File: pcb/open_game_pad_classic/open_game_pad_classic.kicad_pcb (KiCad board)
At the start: 2 copper layers, 140 x 70 mm, 41 parts, among them J1 COM-09032, J2 COM-09032, U1 MM74C923, U2 74HC4051, U3 SN74AHC1G04DBVR

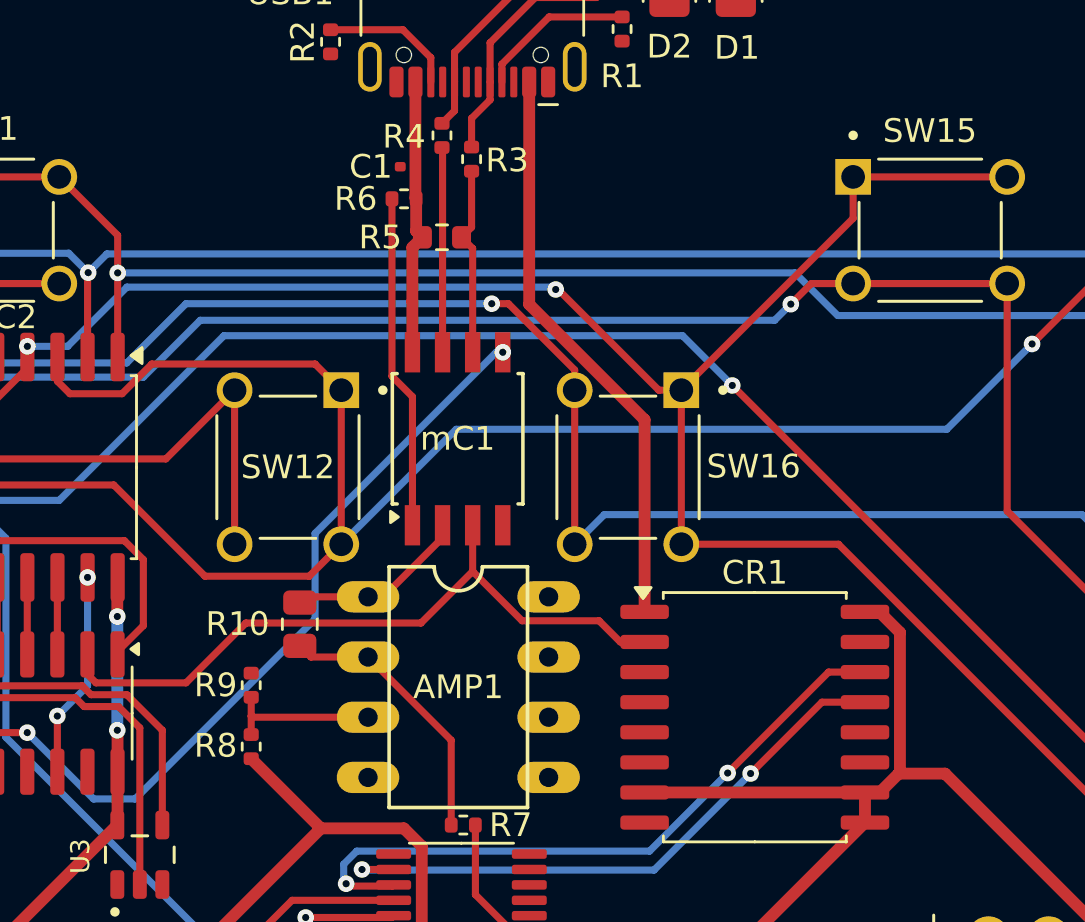
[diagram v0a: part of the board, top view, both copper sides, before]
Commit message: More decoupling for microcontroller and timer.
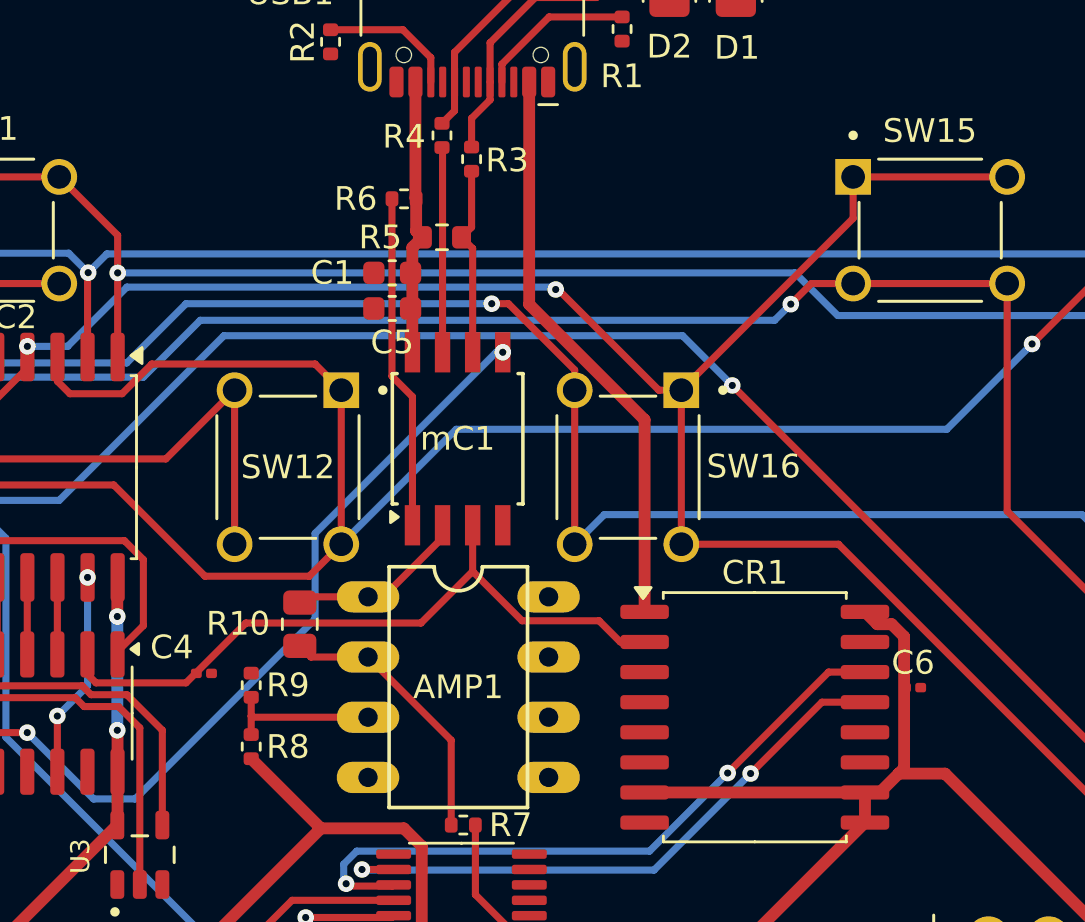
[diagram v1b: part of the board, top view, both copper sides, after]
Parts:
- added C4: 10 pF, Capacitor_SMD:C_0201_0603Metric, F.Cu at (134.4, 88.7)
- added C5: 10 µF, Capacitor_SMD:C_0603_1608Metric, F.Cu at (142.3, 73.3)
- added C6: 100nF, Capacitor_SMD:C_0201_0603Metric, F.Cu at (164.3, 89.3)
- C1: footprint Capacitor_SMD:C_0201_0603Metric -> Capacitor_SMD:C_0603_1608Metric
- moved C1 4.53 mm to (142.3, 71.8)

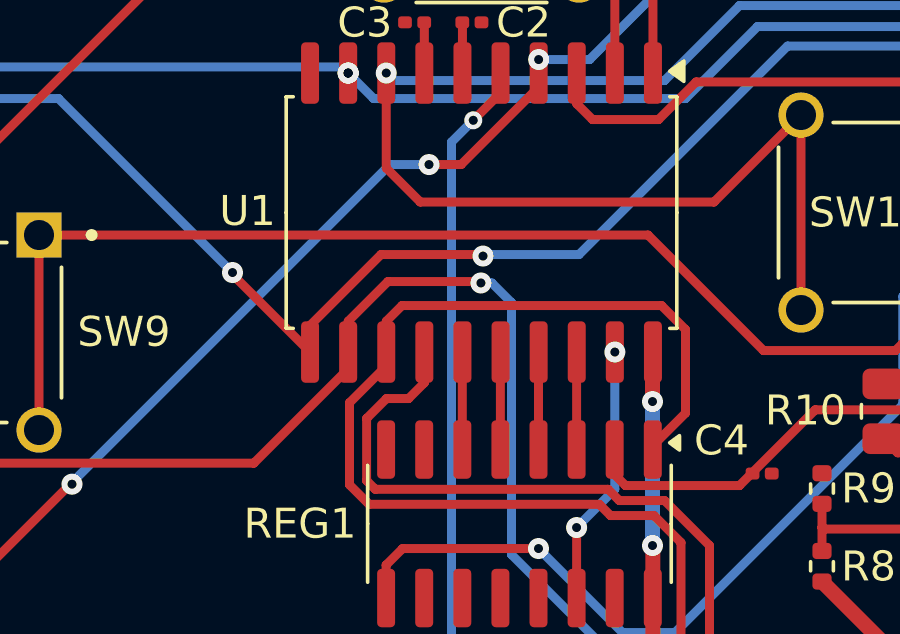
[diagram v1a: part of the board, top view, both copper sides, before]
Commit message: Fixed the schematic on PISO read. Updated the PCB.
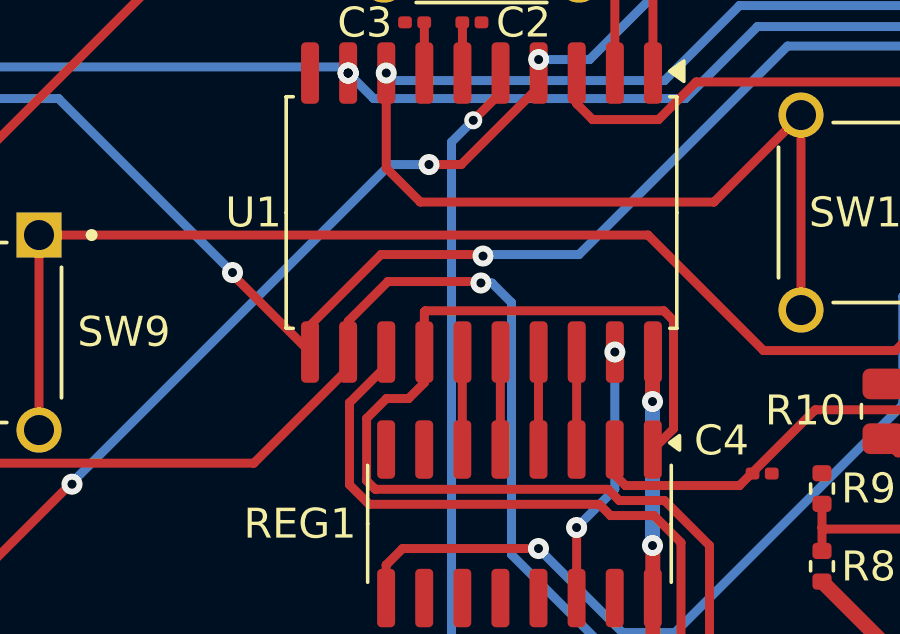
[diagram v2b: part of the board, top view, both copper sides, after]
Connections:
- U1 pad 13: Net-(REG1-~{PL}) -> Net-(U1-DA)
- U1 pad 14: Net-(U1-XOE) -> Net-(REG1-~{PL})
- U3 pad 2: Net-(REG1-~{PL}) -> Net-(U1-DA)
- U3 pad 4: Net-(U1-XOE) -> Net-(REG1-~{PL})
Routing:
- net Net-(U1-DA): track 0.00 -> 23.4 mm
- net Net-(U1-XOE): track 21.8 -> 0.00 mm
- net Net-(REG1-~{PL}): track 39.3 -> 36.2 mm

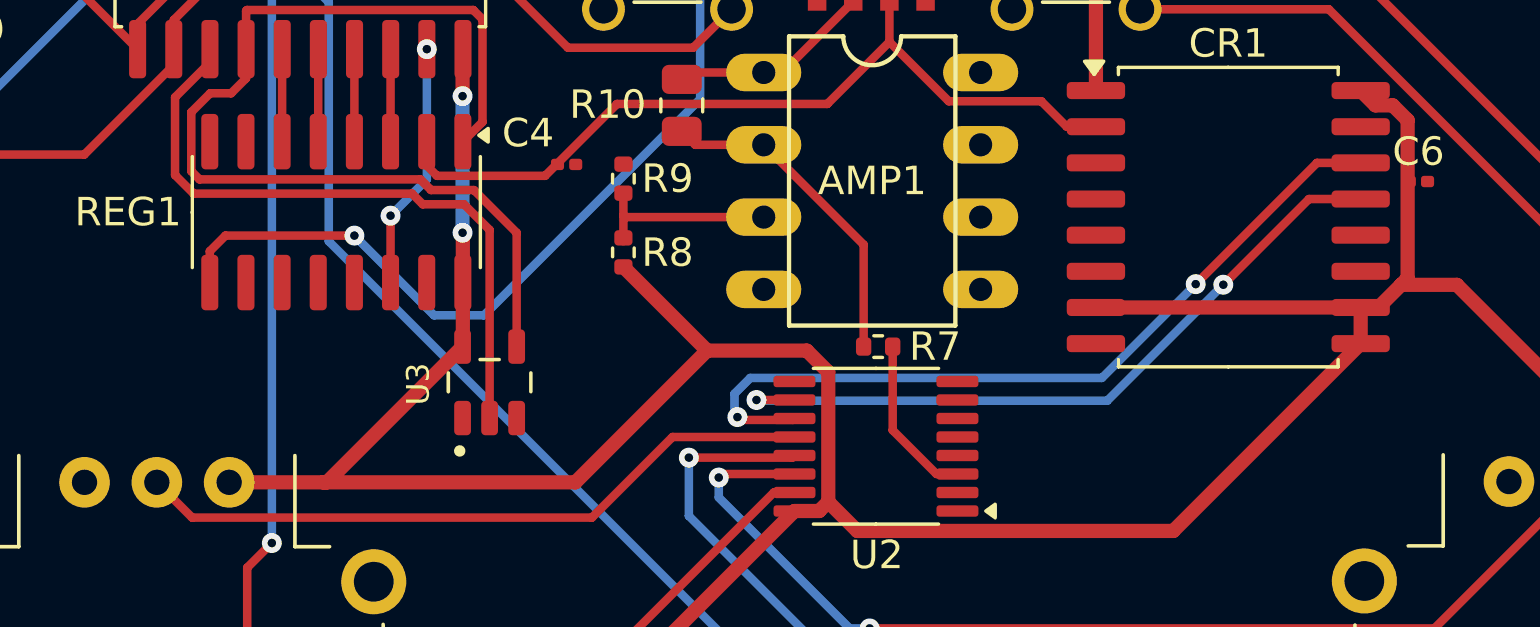
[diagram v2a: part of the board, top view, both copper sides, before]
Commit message: Fixed the reset problem by adding an 8-tick delay.
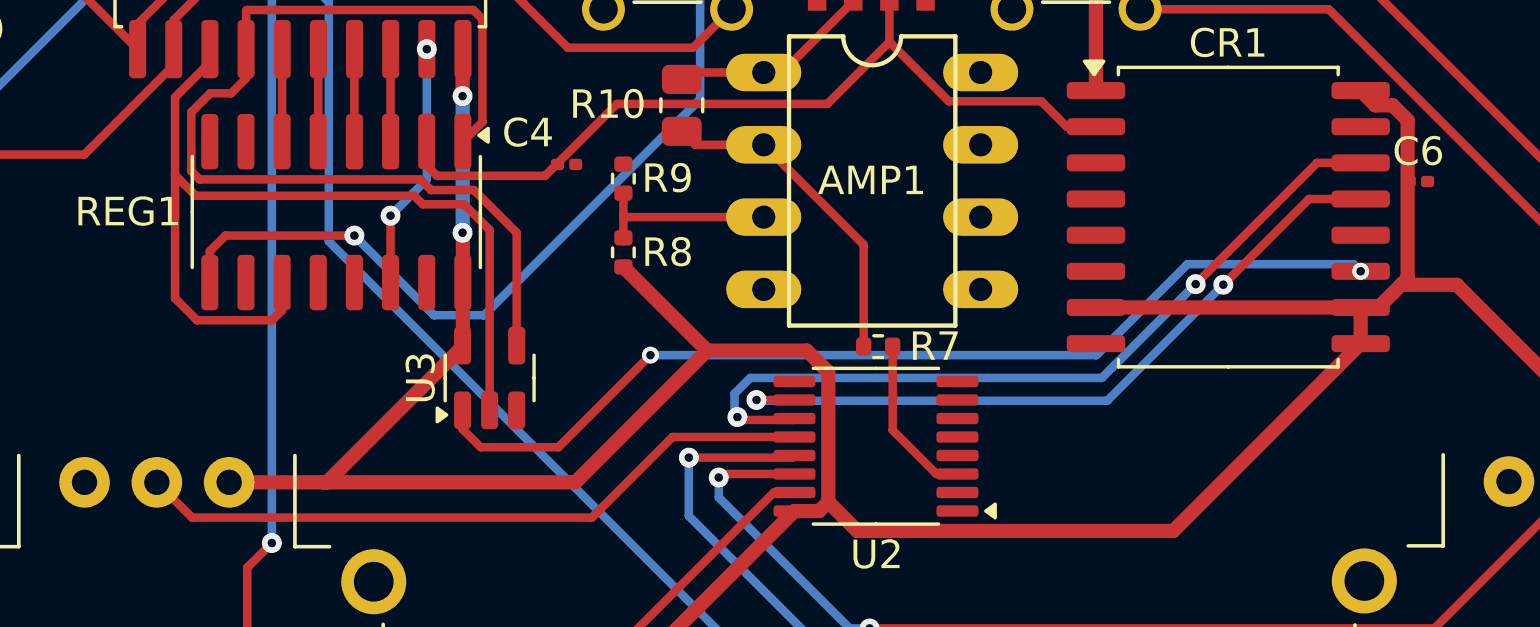
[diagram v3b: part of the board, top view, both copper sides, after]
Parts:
- U3: value SN74AHC1G04DBVR -> 74AHC1G00; footprint SN74AHC1G04DBVR:SOT95P280X145-5N -> Package_TO_SOT_SMD:SOT-23-5
- moved U3 0.16 mm to (131.7, 96.2)
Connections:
- CR1 pad 11: unconnected-(CR1-Q3-Pad11) -> /8TICK
- REG1 pad 11: GND -> Net-(REG1-D0)
- U1 pad 13: Net-(U1-DA) -> Net-(REG1-D0)
- U3 pad 1: unconnected-(U3-Pad1) -> /8TICK
- U3 pad 2: Net-(U1-DA) -> Net-(REG1-D0)
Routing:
- net /8TICK: track 0.00 -> 35.2 mm, vias 0 -> 2
- net Net-(REG1-D0): track 0.00 -> 32.9 mm
- net Net-(U1-DA): track 23.4 -> 0.00 mm

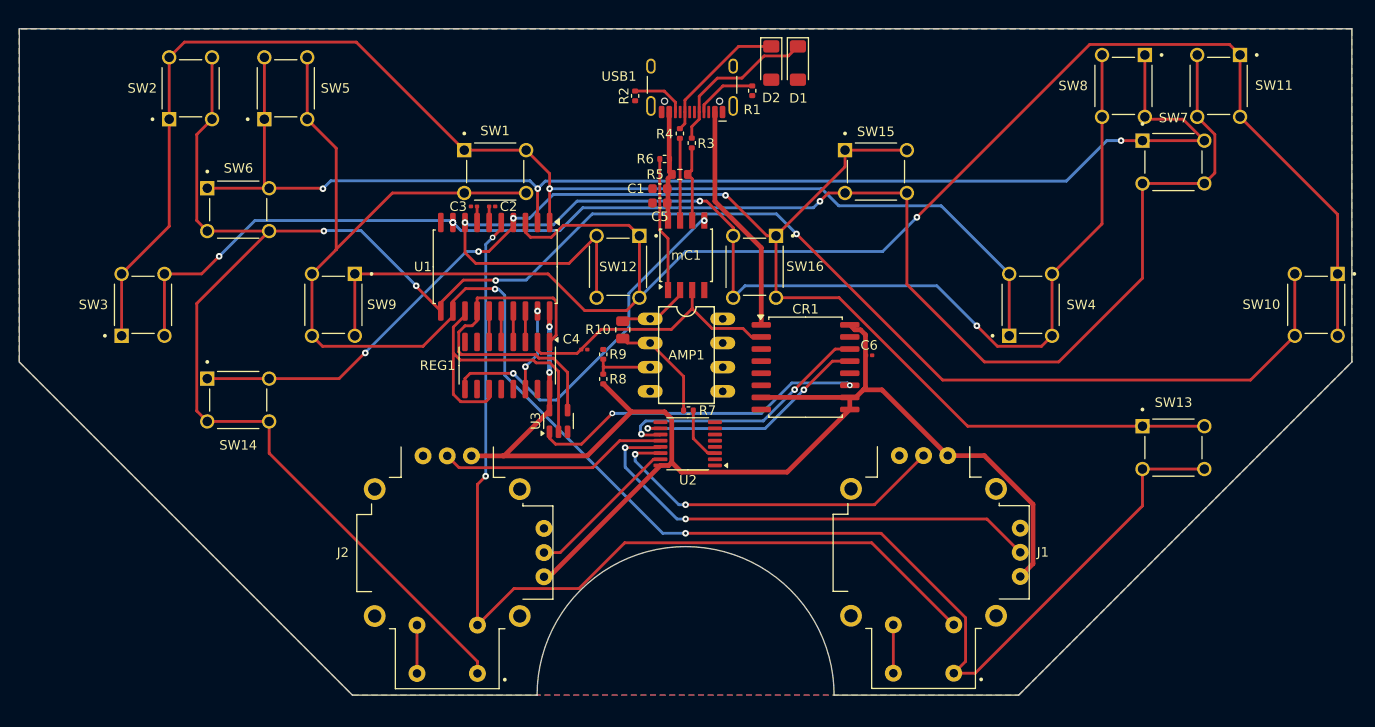
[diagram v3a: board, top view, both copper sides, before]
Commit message: Updated the PCB based on the new schematic design.
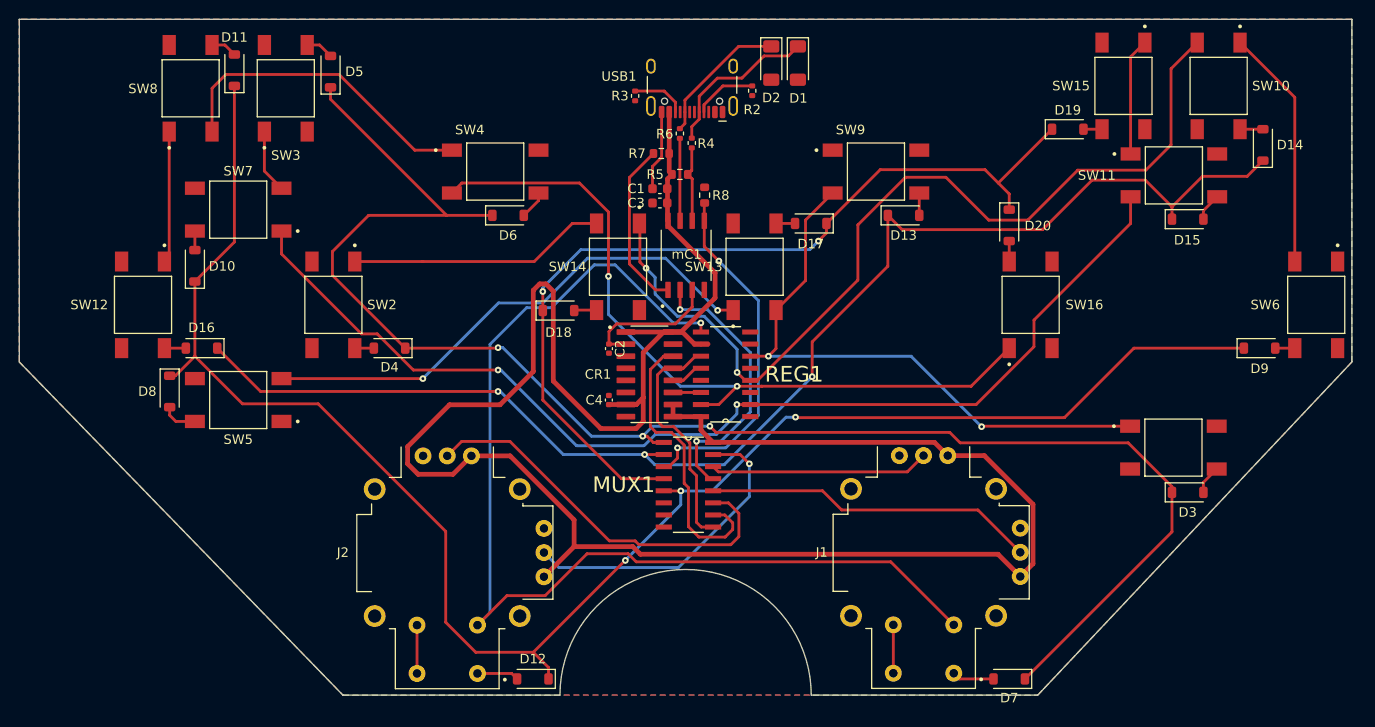
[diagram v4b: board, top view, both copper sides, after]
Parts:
- removed AMP1: LM358, LM358:DIL8
- removed the C3 at (122.8, 73.7)
- removed C6: 100nF, Capacitor_SMD:C_0201_0603Metric
- removed R10: R 10K, Resistor_SMD:R_0805_2012Metric
- removed the R7 at (145.3, 95.1)
- removed R9: R 4.7K, Resistor_SMD:R_0402_1005Metric
- removed U1: MM74C923, Package_SO:SOIC-20W_7.5x12.8mm_P1.27mm
- removed U2: 74HC4051, Package_SO:TSSOP-16_4.4x5mm_P0.65mm
- removed U3: 74AHC1G00, Package_TO_SOT_SMD:SOT-23-5
- added D10: 1N4148W, Diode_SMD:D_SOD-123, F.Cu at (93.5, 79.9)
- added D11: 1N4148W, Diode_SMD:D_SOD-123, F.Cu at (97.6, 59.4)
- added D12: 1N4148W, Diode_SMD:D_SOD-123, F.Cu at (128.9, 123.3)
- added D13: 1N4148W, Diode_SMD:D_SOD-123, F.Cu at (167.9, 74.6)
- added D14: 1N4148W, Diode_SMD:D_SOD-123, F.Cu at (205.7, 67.2)
- added D15: 1N4148W, Diode_SMD:D_SOD-123, F.Cu at (197.8, 75.0)
- added D16: 1N4148W, Diode_SMD:D_SOD-123, F.Cu at (94.2, 88.5)
- added D17: 1N4148W, Diode_SMD:D_SOD-123, F.Cu at (158.2, 75.5)
- added D18: 1N4148W, Diode_SMD:D_SOD-123, F.Cu at (131.7, 84.6)
- added D19: 1N4148W, Diode_SMD:D_SOD-123, F.Cu at (185.2, 65.5)
- added D20: 1N4148W, Diode_SMD:D_SOD-123, F.Cu at (179.0, 75.7)
- added D3: 1N4148W, Diode_SMD:D_SOD-123, F.Cu at (197.8, 103.7)
- added D4: 1N4148W, Diode_SMD:D_SOD-123, F.Cu at (113.9, 88.5)
- added D5: 1N4148W, Diode_SMD:D_SOD-123, F.Cu at (107.7, 59.5)
- added D6: 1N4148W, Diode_SMD:D_SOD-123, F.Cu at (126.3, 74.6)
- added D7: 1N4148W, Diode_SMD:D_SOD-123, F.Cu at (179.0, 123.3)
- added D8: 1N4148W, Diode_SMD:D_SOD-123, F.Cu at (90.8, 93.1)
- added D9: 1N4148W, Diode_SMD:D_SOD-123, F.Cu at (205.3, 88.5)
- added MUX1: 74HC4052D_653, 74HC4052D_653:SOIC127P600X175-16N, F.Cu at (145.3, 102.9)
- C2: value 0.01 mkF -> 10 pF; footprint Capacitor_SMD:C_0201_0603Metric -> Capacitor_SMD:C_0402_1005Metric
- C4: value 10 pF -> 100nF; footprint Capacitor_SMD:C_0201_0603Metric -> Capacitor_SMD:C_0402_1005Metric
- CR1: footprint Package_SO:SOIC-16W_7.5x10.3mm_P1.27mm -> SN74HC163DR:SOIC127P600X175-16N
- R7: renamed from R6; footprint Resistor_SMD:R_0402_1005Metric -> Resistor_SMD:R_0603_1608Metric
- R8: value R 4.7K -> R 1.5K; footprint Resistor_SMD:R_0402_1005Metric -> Resistor_SMD:R_0603_1608Metric
- REG1: value 74HC165 -> 74HC595; footprint Package_SO:SOIC-16_3.9x9.9mm_P1.27mm -> 74HC595DR:SOIC127P600X175-16N
- SW1: renamed from SW13; footprint TS02-66-95-BK-260-LCR-D:SW_TS02-66-95-BK-260-LCR-D -> TS04-66-95-BK-100-SMT:SW_TS04-66-95-BK-100-SMT
- SW10: renamed from SW11; footprint TS02-66-95-BK-260-LCR-D:SW_TS02-66-95-BK-260-LCR-D -> TS04-66-95-BK-100-SMT:SW_TS04-66-95-BK-100-SMT
- SW11: renamed from SW7; footprint TS02-66-95-BK-260-LCR-D:SW_TS02-66-95-BK-260-LCR-D -> TS04-66-95-BK-100-SMT:SW_TS04-66-95-BK-100-SMT
- SW12: renamed from SW3; footprint TS02-66-95-BK-260-LCR-D:SW_TS02-66-95-BK-260-LCR-D -> TS04-66-95-BK-100-SMT:SW_TS04-66-95-BK-100-SMT
- SW13: renamed from SW16; footprint TS02-66-95-BK-260-LCR-D:SW_TS02-66-95-BK-260-LCR-D -> TS04-66-95-BK-100-SMT:SW_TS04-66-95-BK-100-SMT
- SW14: renamed from SW12; footprint TS02-66-95-BK-260-LCR-D:SW_TS02-66-95-BK-260-LCR-D -> TS04-66-95-BK-100-SMT:SW_TS04-66-95-BK-100-SMT
- SW15: renamed from SW8; footprint TS02-66-95-BK-260-LCR-D:SW_TS02-66-95-BK-260-LCR-D -> TS04-66-95-BK-100-SMT:SW_TS04-66-95-BK-100-SMT
- SW16: renamed from SW4; footprint TS02-66-95-BK-260-LCR-D:SW_TS02-66-95-BK-260-LCR-D -> TS04-66-95-BK-100-SMT:SW_TS04-66-95-BK-100-SMT
- SW2: renamed from SW9; footprint TS02-66-95-BK-260-LCR-D:SW_TS02-66-95-BK-260-LCR-D -> TS04-66-95-BK-100-SMT:SW_TS04-66-95-BK-100-SMT
- SW3: renamed from SW5; footprint TS02-66-95-BK-260-LCR-D:SW_TS02-66-95-BK-260-LCR-D -> TS04-66-95-BK-100-SMT:SW_TS04-66-95-BK-100-SMT
- SW4: renamed from SW1; footprint TS02-66-95-BK-260-LCR-D:SW_TS02-66-95-BK-260-LCR-D -> TS04-66-95-BK-100-SMT:SW_TS04-66-95-BK-100-SMT
- SW5: renamed from SW14; footprint TS02-66-95-BK-260-LCR-D:SW_TS02-66-95-BK-260-LCR-D -> TS04-66-95-BK-100-SMT:SW_TS04-66-95-BK-100-SMT
- SW6: renamed from SW10; footprint TS02-66-95-BK-260-LCR-D:SW_TS02-66-95-BK-260-LCR-D -> TS04-66-95-BK-100-SMT:SW_TS04-66-95-BK-100-SMT
- SW7: renamed from SW6; footprint TS02-66-95-BK-260-LCR-D:SW_TS02-66-95-BK-260-LCR-D -> TS04-66-95-BK-100-SMT:SW_TS04-66-95-BK-100-SMT
- SW8: renamed from SW2; footprint TS02-66-95-BK-260-LCR-D:SW_TS02-66-95-BK-260-LCR-D -> TS04-66-95-BK-100-SMT:SW_TS04-66-95-BK-100-SMT
- SW9: renamed from SW15; footprint TS02-66-95-BK-260-LCR-D:SW_TS02-66-95-BK-260-LCR-D -> TS04-66-95-BK-100-SMT:SW_TS04-66-95-BK-100-SMT
- mC1: footprint Package_SO:SOIC-8W_5.3x5.3mm_P1.27mm -> ATTINY85-20SU:SOIC127P798X216-8N
- moved REG1 23.0 mm to (149.2, 91.3), turned to 180 degrees
- moved R8 22.1 mm to (147.0, 72.5), turned to -90 degrees
- moved C2 19.3 mm to (136.9, 88.6), turned to -90 degrees
- moved CR1 16.4 mm to (141.2, 91.3)
- moved C4 5.90 mm to (136.9, 94.0), turned to 90 degrees
- moved SW11 1.40 mm to (196.3, 70.4)
- moved R7 0.67 mm to (142.4, 68.1)
- turned SW12 to -90 degrees
- turned SW13 to 90 degrees
- turned SW5 to 180 degrees
- turned SW7 to 180 degrees
- renumbered C5 to C3, R1 to R2, R2 to R3, R3 to R4, R4 to R6
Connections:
- C2 pad 1: Net-(U1-OSC) -> /CLK
- C4 pad 1: /CLK -> +5V
- CR1 pad 11: /8TICK -> /CLK/16
- CR1 pad 12: unconnected-(CR1-Q2-Pad12) -> /CLK/8
- CR1 pad 13: Net-(CR1-Q1) -> /CLK/4
- J1 pad B1A: /X1 -> /X1J
- J2 pad B1A: /X2 -> /X2J
- R8 pad 1: +5V -> GND
- R8 pad 2: Net-(AMP1-Pad3) -> /DIN
- REG1 pad 1: Net-(REG1-~{PL}) -> unconnected-(REG1-QB-Pad1)
- REG1 pad 10: GND -> +5V
- REG1 pad 11: Net-(REG1-D0) -> /CLK/4
- REG1 pad 12: GND -> /CLK/8
- REG1 pad 14: Net-(REG1-D3) -> /CLK/16
- REG1 pad 15: GND -> /Y1
- REG1 pad 2: /CLK -> /Y2
- REG1 pad 3: Net-(REG1-D4) -> unconnected-(REG1-QD-Pad3)
- REG1 pad 4: Net-(REG1-D5) -> /Y3
- REG1 pad 5: Net-(REG1-D6) -> unconnected-(REG1-QF-Pad5)
- REG1 pad 6: Net-(REG1-D7) -> /Y4
- REG1 pad 9: /DIN -> /Y5
- SW1 pad 3: /X1 -> Net-(D3-A)
- SW1 pad 4: /X1 -> Net-(D3-A)
- SW10 pad 3: /X3 -> Net-(D14-A)
- SW10 pad 4: /X3 -> Net-(D14-A)
- SW11 pad 3: /X3 -> Net-(D15-A)
- SW11 pad 4: /X3 -> Net-(D15-A)
- SW12 pad 3: /X3 -> Net-(D16-A)
- SW12 pad 4: /X3 -> Net-(D16-A)
- SW13 pad 3: /X4 -> Net-(D17-A)
- SW13 pad 4: /X4 -> Net-(D17-A)
- SW14 pad 3: /X4 -> Net-(D18-A)
- SW14 pad 4: /X4 -> Net-(D18-A)
- SW15 pad 3: /X4 -> Net-(D19-A)
- SW15 pad 4: /X4 -> Net-(D19-A)
- SW16 pad 3: /X4 -> Net-(D20-A)
- SW16 pad 4: /X4 -> Net-(D20-A)
- SW2 pad 3: /X1 -> Net-(D4-A)
- SW2 pad 4: /X1 -> Net-(D4-A)
- SW3 pad 3: /X1 -> Net-(D5-A)
- SW3 pad 4: /X1 -> Net-(D5-A)
- SW4 pad 3: /X1 -> Net-(D6-A)
- SW4 pad 4: /X1 -> Net-(D6-A)
- SW5 pad 3: /X2 -> Net-(D8-A)
- SW5 pad 4: /X2 -> Net-(D8-A)
- SW6 pad 3: /X2 -> Net-(D9-A)
- SW6 pad 4: /X2 -> Net-(D9-A)
- SW7 pad 3: /X2 -> Net-(D10-A)
- SW7 pad 4: /X2 -> Net-(D10-A)
- SW8 pad 3: /X2 -> Net-(D11-A)
- SW8 pad 4: /X2 -> Net-(D11-A)
- SW9 pad 3: /X3 -> Net-(D13-A)
- SW9 pad 4: /X3 -> Net-(D13-A)
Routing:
- net +5V: track 177.0 -> 230.0 mm, vias 2 -> 0
- net /X2: track 223.3 -> 181.7 mm, vias 4 -> 3
- net /X4: track 131.8 -> 93.4 mm, vias 3 -> 2
- net Net-(REG1-~{PL}): track 36.2 -> 0.00 mm
- net /8TICK: track 35.2 -> 0.00 mm, vias 2 -> 0
- net Net-(REG1-D0): track 32.9 -> 0.00 mm
- net /Y4: track 145.3 -> 117.9 mm
- net Net-(CR1-Q1): track 25.5 -> 0.00 mm, vias 2 -> 0
- net /CLK/4: track 0.00 -> 25.2 mm
- net /X1: track 189.6 -> 166.8 mm, vias 2 -> 3
- net /AIN: track 7.68 -> 29.4 mm, vias 0 -> 2
- net /X3: track 161.4 -> 140.3 mm, vias 4 -> 3
- net /Y3: track 167.6 -> 149.2 mm, vias 1 -> 2
- net Net-(J2-H): track 24.1 -> 41.7 mm
- net Net-(J2-V): track 16.3 -> 33.0 mm, vias 0 -> 1
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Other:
- board size 140 x 70 mm -> 140 x 71 mm
